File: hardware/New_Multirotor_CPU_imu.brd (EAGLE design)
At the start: 52 x 52 mm, 85 parts, among them X2 telemetry, X3 programm, X4 sonar

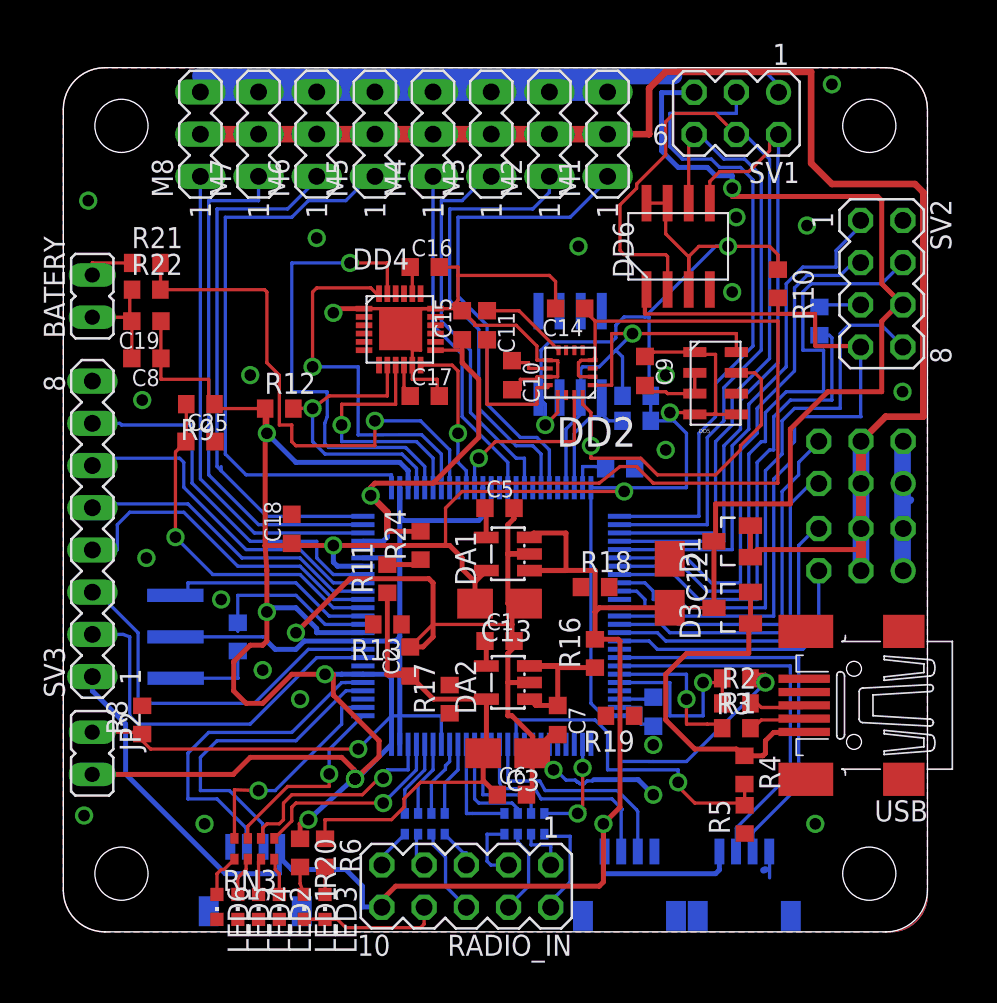
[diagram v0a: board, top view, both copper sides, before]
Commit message: Fixes a bug
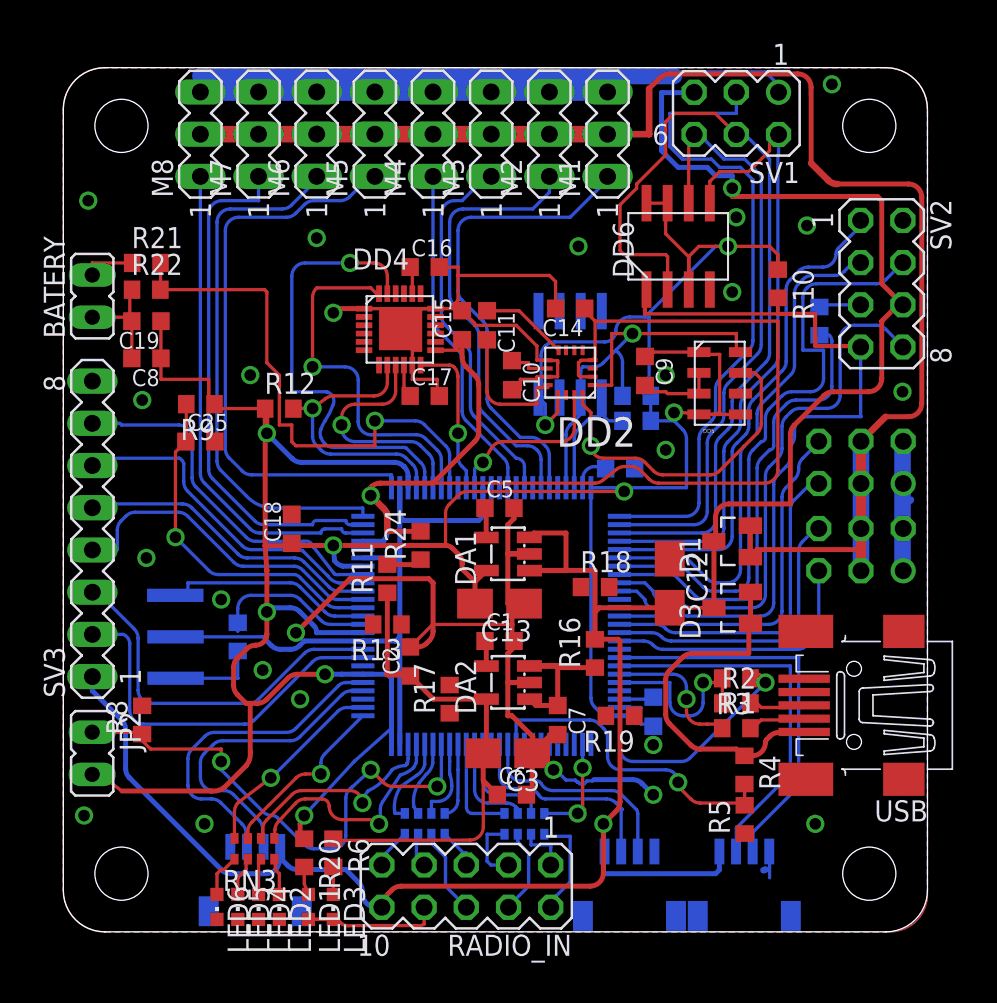
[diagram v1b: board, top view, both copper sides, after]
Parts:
- moved LED3 0.50 mm to (16.2, 1.50)
- moved R6 0.50 mm to (16.2, 4.75)
- moved DD5 0.25 mm to (39.5, 33.0)
- moved LED1 0.25 mm to (14.7, 1.50)
- moved R20 0.25 mm to (14.5, 4.75)
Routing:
- net N$14: track 24.5 -> 0.00 mm
- net N$20: track 95.1 -> 118.2 mm
- net VCC: track 233.1 -> 219.8 mm, vias 12 -> 10
- net N$61: track 24.2 -> 31.4 mm, vias 1 -> 3
- net +5V: track 148.0 -> 145.3 mm
- net N$3: track 12.3 -> 14.1 mm
- net XZ1: track 34.2 -> 32.6 mm
- net MISO: track 15.5 -> 14.0 mm
- net PPS: track 37.7 -> 36.3 mm
- net N$11: track 13.3 -> 11.9 mm
- net N$29: track 28.9 -> 27.6 mm
- net GPS_TX: track 31.0 -> 29.7 mm
- net XZ2: track 48.1 -> 46.9 mm
- net MOSI: track 23.1 -> 22.0 mm
- net ADC4: track 22.7 -> 21.6 mm
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
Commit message: Перезалил
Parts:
- removed R11: 0, resistor:R0603
- moved C26 1.00 mm to (35.5, 12.2)
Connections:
- removed net N$15: R11.2, R24.1
- removed net XZ1: DD1.59, SV2.8
- removed net XZ2: DD1.60, DD6.1, R10.2, SV2.7
- new net CS_FLASH: DD1.60, DD6.1, R10.2
- net +5V: now also RADIO_IN.8; no longer RADIO_IN.10
- net GND: now also RADIO_IN.10; no longer RADIO_IN.8
- net N$7: now also R24.1; no longer R11.1
- net XZ3: now also SV2.7
- net XZ4: now also SV2.8
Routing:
- net XZ2: track 46.9 -> 0.00 mm
- net CS_FLASH: track 0.00 -> 39.2 mm, vias 0 -> 1
- net XZ1: track 32.6 -> 0.00 mm
- net XZ4: track 0.00 -> 26.9 mm
- net XZ3: track 0.00 -> 25.5 mm
- net N$18: track 0.00 -> 10.2 mm
- net P_RX: track 22.8 -> 30.3 mm
- net P_TX: track 23.5 -> 30.8 mm
- net N$47: track 21.6 -> 14.6 mm
- net N$41: track 8.31 -> 14.5 mm
- net N$14: track 0.00 -> 5.02 mm
- net GND: track 235.6 -> 230.7 mm, vias 24 -> 30
- net SERVO_2: track 19.8 -> 15.5 mm
- net PPS: track 36.3 -> 32.1 mm
- net N$29: track 27.6 -> 23.5 mm
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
